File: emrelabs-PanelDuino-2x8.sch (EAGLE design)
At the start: 64 parts, among them CN1 USB-MICROB, CN11 AVR-ICSP, U1 7805, U3 CH340G, U4 PCF8574, U5 ATMEGA328PA, U6 PCF8574

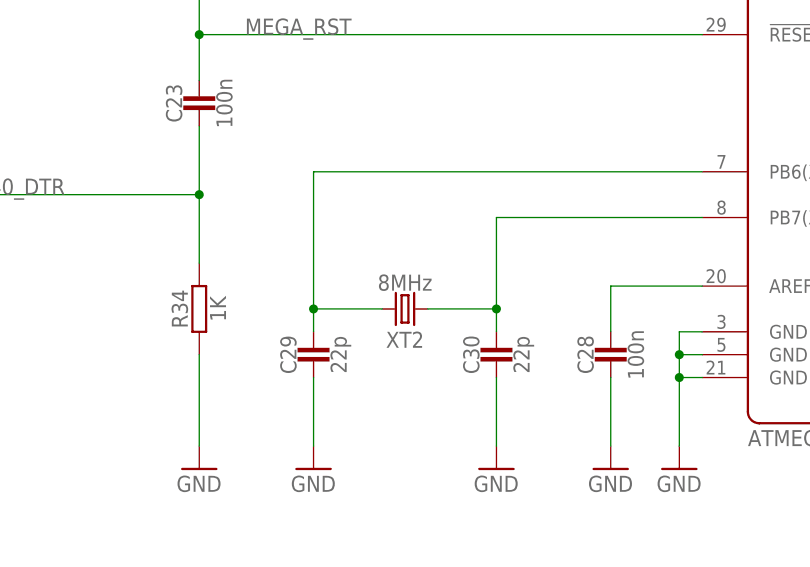
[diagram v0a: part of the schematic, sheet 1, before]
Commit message: Crystal value updated
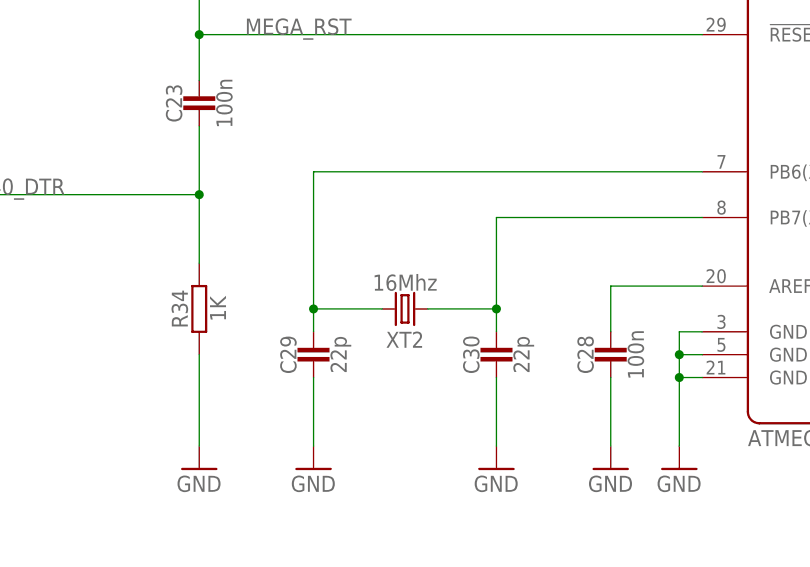
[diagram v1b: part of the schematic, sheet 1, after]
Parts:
- XT2: value 8MHz -> 16Mhz
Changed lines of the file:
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@@
 <part name="C27" library="Elib-RLC-D-XT" deviceset="C?-*" device="1206" technology="100N" value="100n"/>
 <part name="GND36" library="supply1" library_urn="urn:adsk.eagle:library:371" deviceset="GND" device=""/>
-<part name="XT2" library="Elib-RLC-D-XT" deviceset="XT-2PIN" device="-HC49" value="8MHz"/>
+<part name="XT2" library="Elib-RLC-D-XT" deviceset="XT-2PIN" device="-HC49" value="16Mhz"/>
 <part name="C28" library="Elib-RLC-D-XT" deviceset="C?-*" device="1206" technology="100N" value="100n"/>
 <part name="GND37" library="supply1" library_urn="urn:adsk.eagle:library:371" deviceset="GND" device=""/>
